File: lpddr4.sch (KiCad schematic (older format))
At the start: 44 parts, among them U1 MT53E1G32D2NP-046

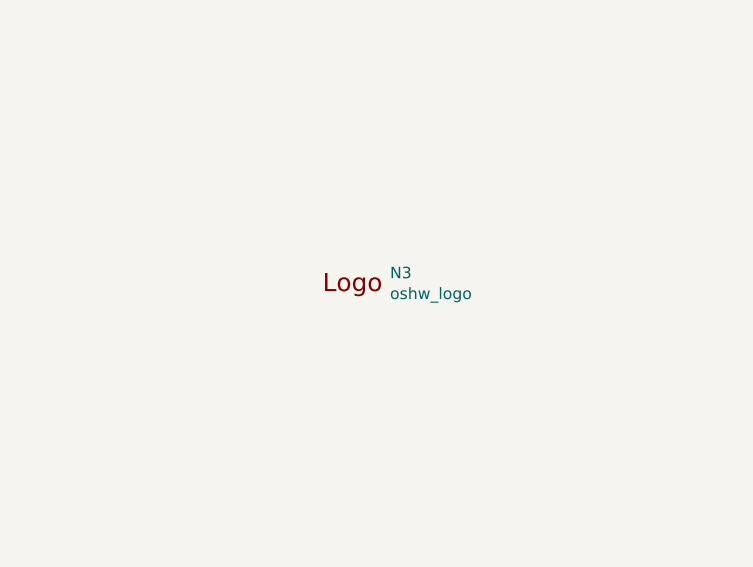
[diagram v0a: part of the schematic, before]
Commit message: Replace broken component -PCA6408APW
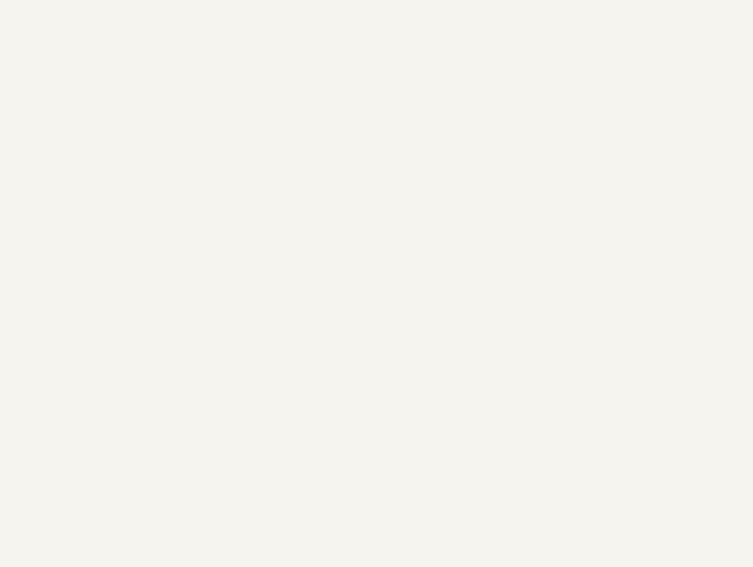
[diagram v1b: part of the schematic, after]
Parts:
- removed N3: oshw_logo, lpddr4-testbed-footprints:oshw-logo, symbol lpddr4-testbed:oshw_logo
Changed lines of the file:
@@
 	12050 3450 12050 3525
-$Comp
-L lpddr4-testbed:oshw_logo N3
-U 1 1 6001ECE6
-P 11900 9575
-F 0 "N3" H 12094 9578 50  0000 L CNN
-F 1 "oshw_logo" H 12094 9487 50  0000 L CNN
-F 2 "lpddr4-testbed-footprints:oshw-logo" H 11920 9335 50  0001 C CNN
-F 3 "" H 11900 9575 50  0001 C CNN
-	1    11900 9575
-	1    0    0    -1
-$EndComp
 $Comp
 L lpddr4-testbed:MT53E1G32D2NP-046 U1
